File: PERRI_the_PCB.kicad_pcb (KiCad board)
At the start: 2 copper layers, 163 x 100 mm, 42 parts, among them J1 SS5-80-3.00-X-D-K-XX, J2 Conn_01x02, J3 Conn_02x50_Counter_Clockwise, J4 Conn_02x05_Counter_Clockwise, J5 SS5-80-3.00-X-D-K-XX, J6 Conn_01x03, J7 Conn_01x03, J8 Conn_01x03, SW2 SW_DIP_x08, U1 TMP441AIDCNR, U2 TPS2595, U3 PCA9554ADB, U4 NCV8508

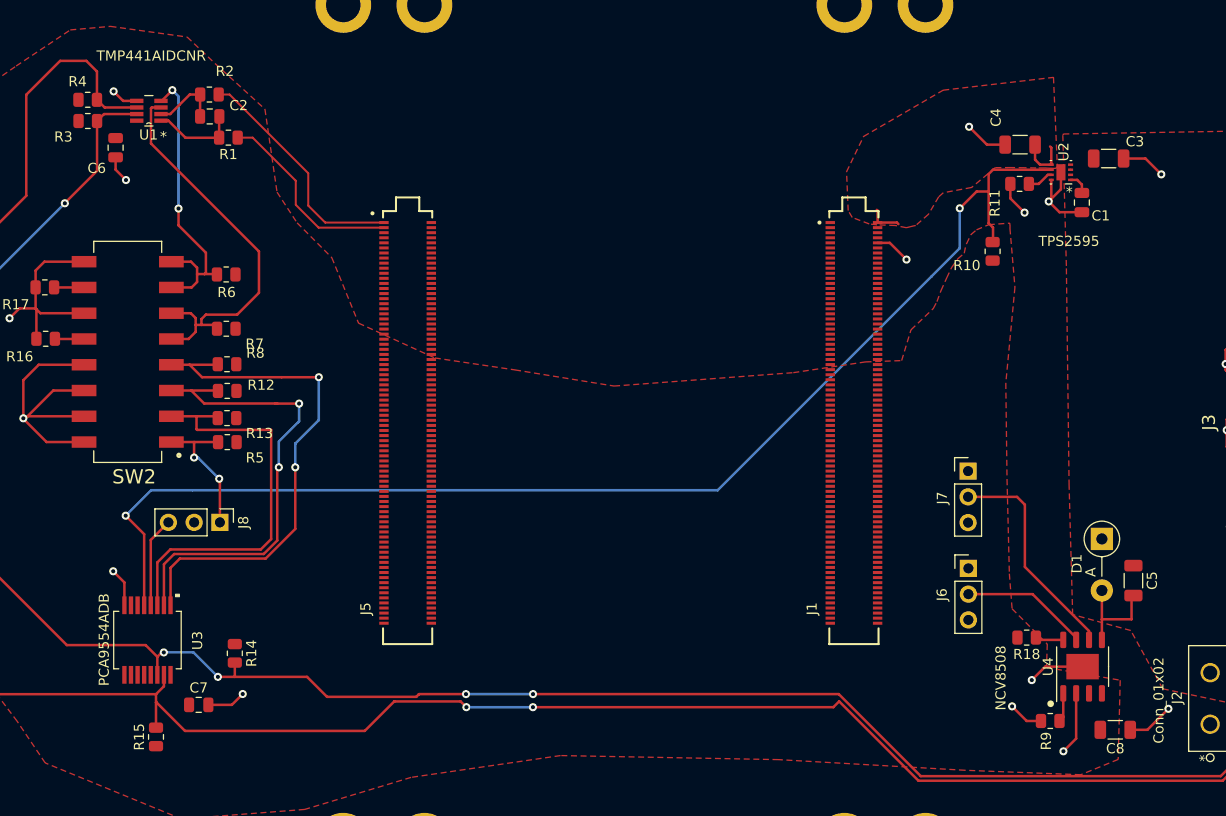
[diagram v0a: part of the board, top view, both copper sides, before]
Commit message: Fixed some alignment issues
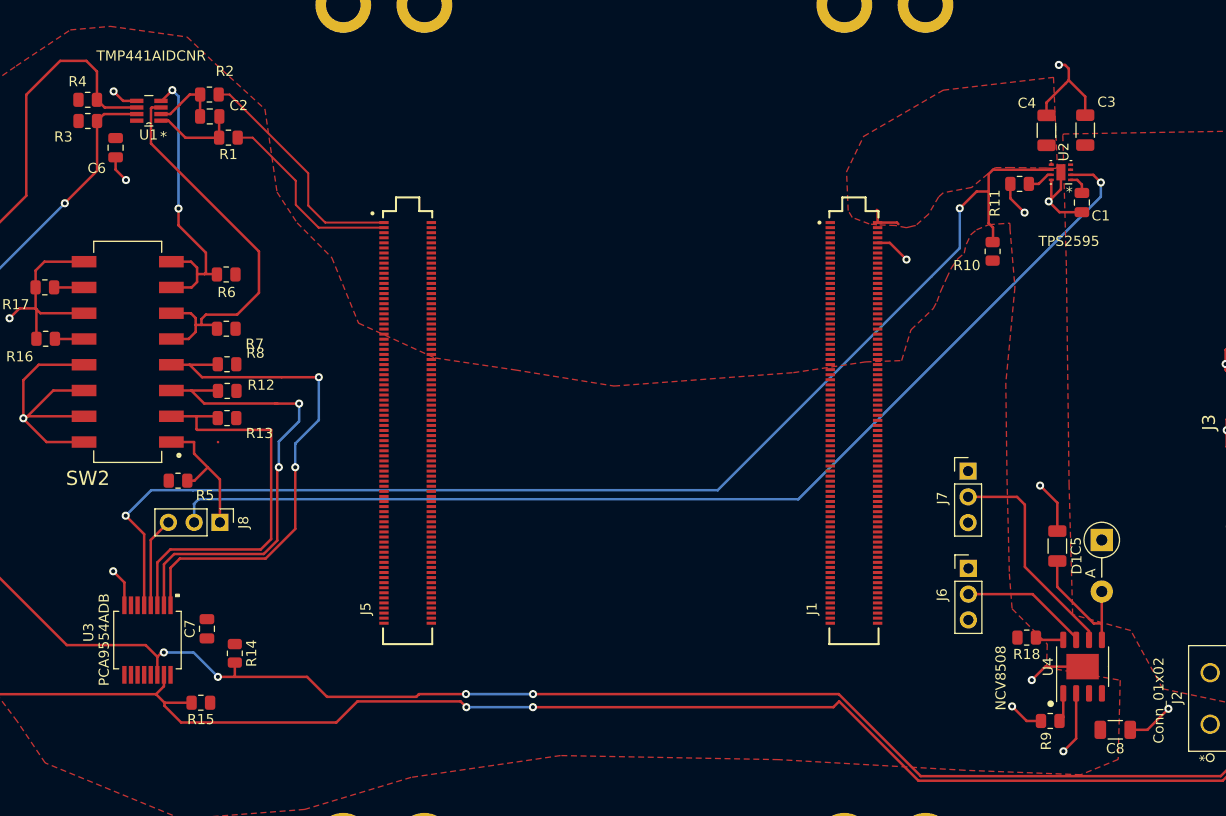
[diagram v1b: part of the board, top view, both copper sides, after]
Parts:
- moved C5 8.24 mm to (222.1, 108.4)
- moved C7 7.54 mm to (138.2, 116.5), turned to 90 degrees
- moved R5 6.17 mm to (135.4, 101.9), turned to 180 degrees
- moved R15 5.56 mm to (137.6, 123.8), turned to 180 degrees
- moved C3 3.63 mm to (224.8, 67.4), turned to 90 degrees
- moved C4 2.96 mm to (221.0, 67.4), turned to 90 degrees
- moved D1 0.11 mm to (226.5, 107.8)
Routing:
- net /To_Efuse_EN: track 0.00 -> 108.5 mm, vias 0 -> 1
- net /12V_To_Hat: track 8.64 -> 3.68 mm
- net GND: track 212.4 -> 215.8 mm, vias 23 -> 22
- net Net-(C5-Pad2): track 10.2 -> 13.2 mm
- net /SDA: track 297.7 -> 296.9 mm
- net /DS_EN: vias 2 -> 0
